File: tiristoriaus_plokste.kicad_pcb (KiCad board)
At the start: 2 copper layers, 33 x 31 mm, 26 parts, among them X1 Faston_6.3x08x14, X2 Faston_6.3x08x14, X3 Faston_6.3x08x14

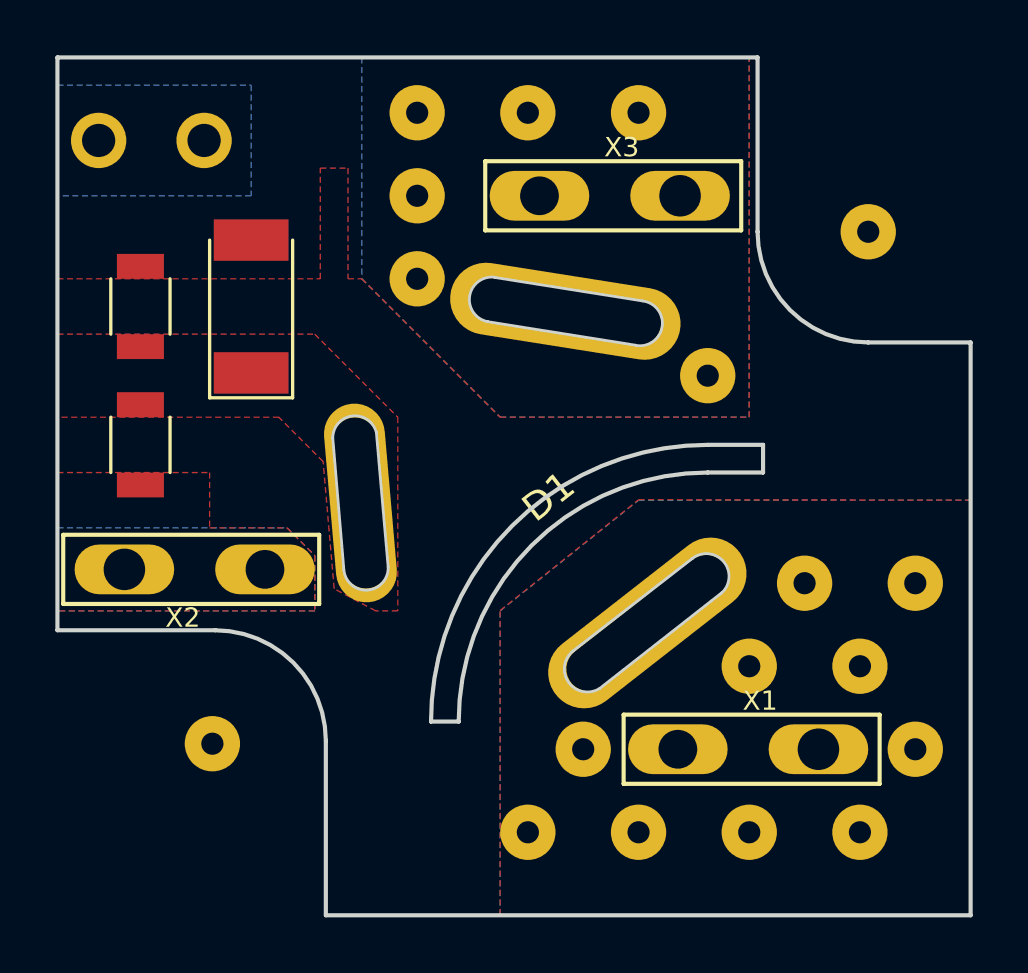
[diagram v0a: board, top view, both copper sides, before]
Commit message: plokstes dviem tiristoriams projektavimas. gerber failu ruosimas gamybai
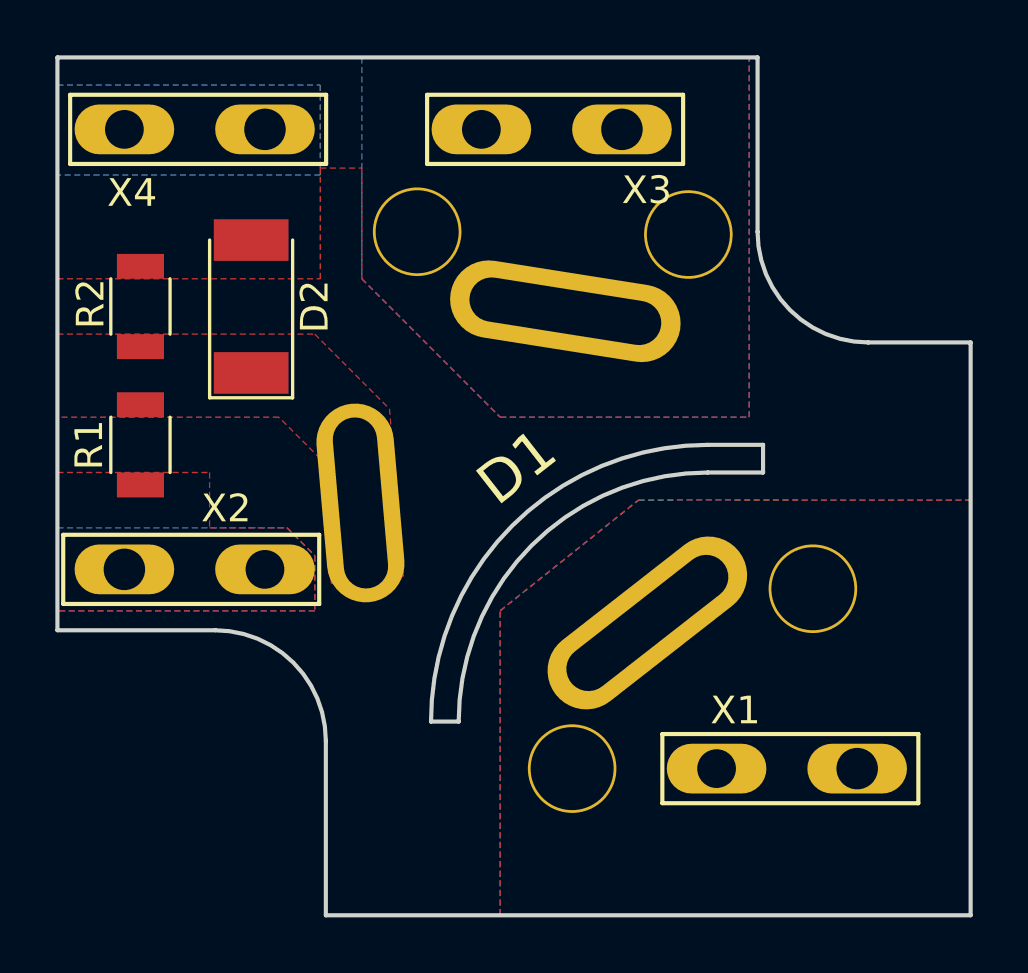
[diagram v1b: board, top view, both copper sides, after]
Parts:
- removed the REF** at (139.3, 101.3)
- removed the REF** at (139.0, 123.0)
- removed the REF** at (135.0, 123.0)
- removed the REF** at (131.0, 123.0)
- removed the REF** at (129.0, 120.0)
- removed the REF** at (141.0, 120.0)
- removed the REF** at (135.0, 117.0)
- removed the REF** at (141.0, 114.0)
- removed the REF** at (113.4, 98.0)
- removed the REF** at (137.0, 114.0)
- removed the REF** at (115.6, 119.8)
- removed the REF** at (133.5, 106.5)
- removed the REF** at (127.0, 123.0)
- removed the REF** at (123.0, 103.0)
- removed the REF** at (123.0, 100.0)
- removed the REF** at (131.0, 97.0)
- removed the REF** at (127.0, 97.0)
- removed the REF** at (123.0, 97.0)
- added REF**: SolderWirePad_single_0-8mmDrill, Wire_Pads:SolderWirePad_single_0-8mmDrill, F.Cu at (132.8, 101.4)
- added REF**: SolderWirePad_single_0-8mmDrill, Wire_Pads:SolderWirePad_single_0-8mmDrill, F.Cu at (128.6, 120.7)
- added REF**: SolderWirePad_single_0-8mmDrill, Wire_Pads:SolderWirePad_single_0-8mmDrill, F.Cu at (123.0, 101.3)
- added X4: Faston_6.3x08x14, mech:Faston_6.3x0.8x14, F.Cu at (115.0, 97.6)
- R1: value 330R -> 470R
- X1: value Faston_6.3x08x14 -> A
- X3: value Faston_6.3x08x14 -> K
- moved REF** 3.28 mm to (137.3, 114.2)
- moved X3 3.19 mm to (127.9, 97.6)
- moved X1 1.57 mm to (136.4, 120.7)
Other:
- outline, holes or cut-outs redrawn
